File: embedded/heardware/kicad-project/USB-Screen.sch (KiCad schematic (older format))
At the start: 19 parts, among them J1 USB_B_Micro, J2 Conn_01x04, U1 ZJY154T-PG04, U2 CH551, U3 XC662

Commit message: pcb完成
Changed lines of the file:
@@
 NoConn ~ 6700 3400
 NoConn ~ 6700 3600
+Text Label 3300 1500 2    50   ~ 0
+USB_D+
 Text Label 3300 1600 2    50   ~ 0
-USB_D+
-Text Label 3300 1500 2    50   ~ 0
 USB_D-
 $Comp
 L power:GND #PWR0106
 U 1 1 5F618012
-P 3300 1700
-F 0 "#PWR0106" H 3300 1450 50  0001 C CNN
-F 1 "GND" H 3305 1527 50  0000 C CNN
-F 2 "" H 3300 1700 50  0001 C CNN
-F 3 "" H 3300 1700 50  0001 C CNN
-	1    3300 1700
-	1    0    0    -1
-$EndComp
-$Comp
-L power:+5V #PWR0105
-U 1 1 5F617214
 P 3300 1400
-F 0 "#PWR0105" H 3300 1250 50  0001 C CNN
-F 1 "+5V" V 3315 1528 50  0000 L CNN
+F 0 "#PWR0106" H 3300 1150 50  0001 C CNN
+F 1 "GND" H 3305 1227 50  0000 C CNN
 F 2 "" H 3300 1400 50  0001 C CNN
 F 3 "" H 3300 1400 50  0001 C CNN
 	1    3300 1400
-	0    1    1    0
+	0    -1   -1   0
 $EndComp
 Wire Wire Line
-	3000 1700 3300 1700
+	3300 1400 3000 1400
 Wire Wire Line
-	3000 1600 3300 1600
+	3300 1500 3000 1500
 Wire Wire Line
-	3000 1500 3300 1500
-Wire Wire Line
-	3000 1400 3300 1400
+	3300 1600 3000 1600
 Text Label 2350 1600 2    50   ~ 0
 USB_D-
@@
 	-1   0    0    1
 $EndComp
+Wire Wire Line
+	3300 1700 3000 1700
+$Comp
+L power:+5V #PWR0105
+U 1 1 5F617214
+P 3300 1700
+F 0 "#PWR0105" H 3300 1550 50  0001 C CNN
+F 1 "+5V" V 3315 1828 50  0000 L CNN
+F 2 "" H 3300 1700 50  0001 C CNN
+F 3 "" H 3300 1700 50  0001 C CNN
+	1    3300 1700
+	0    1    1    0
+$EndComp
 $EndSCHEMATC

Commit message: 微调，打样
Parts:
- U3: value XC662 -> SC662; symbol USB_Screen_Library:XC662 -> USB_Screen_Library:SC662
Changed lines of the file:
@@
 $EndComp
 $Comp
-L USB_Screen_Library:XC662 U3
+L USB_Screen_Library:SC662 U3
 U 1 1 5F61E515
 P 2000 5200
 F 0 "U3" H 2000 5400 50  0000 C CNN
-F 1 "XC662" H 2150 5000 50  0000 C CNN
+F 1 "SC662" H 2150 5000 50  0000 C CNN
 F 2 "Package_TO_SOT_SMD:SOT-23" H 2000 5350 50  0001 C CNN
 F 3 "" H 2000 5350 50  0001 C CNN

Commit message: 更正背光电路
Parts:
- added Q1: NPN, Package_TO_SOT_SMD:SOT-23, symbol Transistor_BJT:2SC4213
- added R6: 33R, Resistor_SMD:R_0402_1005Metric, symbol Device:R
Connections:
- wire segments 66 -> 71
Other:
- moved on the sheet: R2
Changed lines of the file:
@@
 L Device:R R2
 U 1 1 5F66A17C
-P 4500 3900
-F 0 "R2" V 4400 3900 50  0000 C CNN
-F 1 "33R" V 4500 3900 50  0000 C CNN
-F 2 "Resistor_SMD:R_0402_1005Metric" V 4430 3900 50  0001 C CNN
-F 3 "~" H 4500 3900 50  0001 C CNN
-	1    4500 3900
+P 4450 3900
+F 0 "R2" V 4350 3900 50  0000 C CNN
+F 1 "33R" V 4450 3900 50  0000 C CNN
+F 2 "Resistor_SMD:R_0402_1005Metric" V 4380 3900 50  0001 C CNN
+F 3 "~" H 4450 3900 50  0001 C CNN
+	1    4450 3900
 	0    -1   -1   0
 $EndComp
@@
 	1850 3950 1600 3950
 Wire Wire Line
-	4850 3900 4650 3900
-Wire Wire Line
-	4350 3900 4100 3900
-Text Label 4850 3900 2    50   ~ 0
-PWM
-Text Label 4100 3900 0    50   ~ 0
+	4300 3900 4050 3900
+Text Label 4050 3900 0    50   ~ 0
 KEDA
 Wire Wire Line
@@
 	0    1    1    0
 $EndComp
+$Comp
+L power:+5V #PWR0113
+U 1 1 5F724019
+P 4800 3900
+F 0 "#PWR0113" H 4800 3750 50  0001 C CNN
+F 1 "+5V" V 4815 4028 50  0000 L CNN
+F 2 "" H 4800 3900 50  0001 C CNN
+F 3 "" H 4800 3900 50  0001 C CNN
+	1    4800 3900
+	0    1    1    0
+$EndComp
+$Comp
+L Transistor_BJT:2SC4213 Q1
+U 1 1 5F727A10
+P 4500 4600
+F 0 "Q1" H 4691 4554 50  0000 L CNN
+F 1 "NPN" H 4691 4645 50  0000 L CNN
+F 2 "Package_TO_SOT_SMD:SOT-23" H 4700 4525 50  0001 L CIN
+F 3 "https://toshiba.semicon-storage.com/info/docget.jsp?did=19305&prodName=2SC4213" H 4500 4600 50  0001 L CNN
+	1    4500 4600
+	-1   0    0    1
+$EndComp
+$Comp
+L power:+5V #PWR0114
+U 1 1 5F730CBA
+P 4400 5000
+F 0 "#PWR0114" H 4400 4850 50  0001 C CNN
+F 1 "+5V" H 4415 5173 50  0000 C CNN
+F 2 "" H 4400 5000 50  0001 C CNN
+F 3 "" H 4400 5000 50  0001 C CNN
+	1    4400 5000
+	-1   0    0    1
+$EndComp
+Wire Wire Line
+	4400 5000 4400 4800
+Wire Wire Line
+	4800 3900 4600 3900
+Wire Wire Line
+	4400 4250 4400 4400
+Wire Wire Line
+	4700 4600 5000 4600
+Text Label 5000 4600 2    50   ~ 0
+PWM
+Text Label 3450 4250 0    50   ~ 0
+KEDA
+$Comp
+L Device:R R6
+U 1 1 5F74A98E
+P 4000 4250
+F 0 "R6" V 3900 4250 50  0000 C CNN
+F 1 "33R" V 4000 4250 50  0000 C CNN
+F 2 "Resistor_SMD:R_0402_1005Metric" V 3930 4250 50  0001 C CNN
+F 3 "~" H 4000 4250 50  0001 C CNN
+	1    4000 4250
+	0    -1   -1   0
+$EndComp
+Wire Wire Line
+	3450 4250 3850 4250
+Wire Wire Line
+	4150 4250 4400 4250
 $EndSCHEMATC

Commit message: sda、clk加上拉电阻，去掉下载电路焊盘
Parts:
- removed JP1: P3.6 download, Jumper:SolderJumper-2_P1.3mm_Open_Pad1.0x1.5mm, symbol Device:Jumper_NO_Small
- added R7: 10K, Resistor_SMD:R_0402_1005Metric, symbol Device:R
- Q1: symbol Transistor_BJT:2SC4213 -> USB-Screen-rescue:2SC4213-Transistor_BJT
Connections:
- wire segments 71 -> 70
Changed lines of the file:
@@
 EESchema Schematic File Version 4
+LIBS:USB-Screen-cache
 EELAYER 30 0
 EELAYER END
@@
 PWM
 $Comp
-L Device:Jumper_NO_Small JP1
-U 1 1 5F656264
-P 6850 2000
-F 0 "JP1" H 6850 2100 50  0000 C CNN
-F 1 "P3.6 download" H 6800 1950 50  0000 C CNN
-F 2 "Jumper:SolderJumper-2_P1.3mm_Open_Pad1.0x1.5mm" H 6850 2000 50  0001 C CNN
-F 3 "~" H 6850 2000 50  0001 C CNN
-	1    6850 2000
-	1    0    0    -1
-$EndComp
-Wire Wire Line
-	6500 2000 6750 2000
-Wire Wire Line
-	6950 2000 7100 2000
-Text Label 6500 2000 0    50   ~ 0
-USB_D+
-$Comp
-L Device:R R1
-U 1 1 5F662FAB
-P 7250 2000
-F 0 "R1" V 7350 2000 50  0000 C CNN
-F 1 "10K" V 7250 2000 50  0000 C CNN
-F 2 "Resistor_SMD:R_0402_1005Metric" V 7180 2000 50  0001 C CNN
-F 3 "~" H 7250 2000 50  0001 C CNN
-	1    7250 2000
-	0    -1   -1   0
-$EndComp
-$Comp
-L power:+5V #PWR08
-U 1 1 5F663B6A
-P 7600 2000
-F 0 "#PWR08" H 7600 1850 50  0001 C CNN
-F 1 "+5V" V 7615 2128 50  0000 L CNN
-F 2 "" H 7600 2000 50  0001 C CNN
-F 3 "" H 7600 2000 50  0001 C CNN
-	1    7600 2000
-	0    1    1    0
-$EndComp
-Wire Wire Line
-	7400 2000 7600 2000
-$Comp
 L Device:R R2
 U 1 1 5F66A17C
@@
 $EndComp
 $Comp
-L Transistor_BJT:2SC4213 Q1
+L USB-Screen-rescue:2SC4213-Transistor_BJT Q1
 U 1 1 5F727A10
 P 4500 4600
@@
 Wire Wire Line
 	4150 4250 4400 4250
+$Comp
+L Device:R R1
+U 1 1 5F81BAD2
+P 2750 3100
+F 0 "R1" H 2680 3054 50  0000 R CNN
+F 1 "10K" H 2680 3145 50  0000 R CNN
+F 2 "Resistor_SMD:R_0402_1005Metric" V 2680 3100 50  0001 C CNN
+F 3 "~" H 2750 3100 50  0001 C CNN
+	1    2750 3100
+	-1   0    0    1
+$EndComp
+$Comp
+L Device:R R7
+U 1 1 5F81D793
+P 3000 3100
+F 0 "R7" H 3070 3146 50  0000 L CNN
+F 1 "10K" H 3070 3055 50  0000 L CNN
+F 2 "Resistor_SMD:R_0402_1005Metric" V 2930 3100 50  0001 C CNN
+F 3 "~" H 3000 3100 50  0001 C CNN
+	1    3000 3100
+	1    0    0    -1
+$EndComp
+$Comp
+L power:+3.3V #PWR0115
+U 1 1 5F8207AA
+P 2750 2950
+F 0 "#PWR0115" H 2750 2800 50  0001 C CNN
+F 1 "+3.3V" H 2765 3123 50  0000 C CNN
+F 2 "" H 2750 2950 50  0001 C CNN
+F 3 "" H 2750 2950 50  0001 C CNN
+	1    2750 2950
+	1    0    0    -1
+$EndComp
+$Comp
+L power:+3.3V #PWR0116
+U 1 1 5F820FDB
+P 3000 2950
+F 0 "#PWR0116" H 3000 2800 50  0001 C CNN
+F 1 "+3.3V" H 3015 3123 50  0000 C CNN
+F 2 "" H 3000 2950 50  0001 C CNN
+F 3 "" H 3000 2950 50  0001 C CNN
+	1    3000 2950
+	1    0    0    -1
+$EndComp
+Wire Wire Line
+	2750 3250 2750 3500
+Wire Wire Line
+	3000 3250 3000 3500
+Text Label 2750 3500 1    50   ~ 0
+SCL
+Text Label 3000 3500 1    50   ~ 0
+SDA
 $EndSCHEMATC

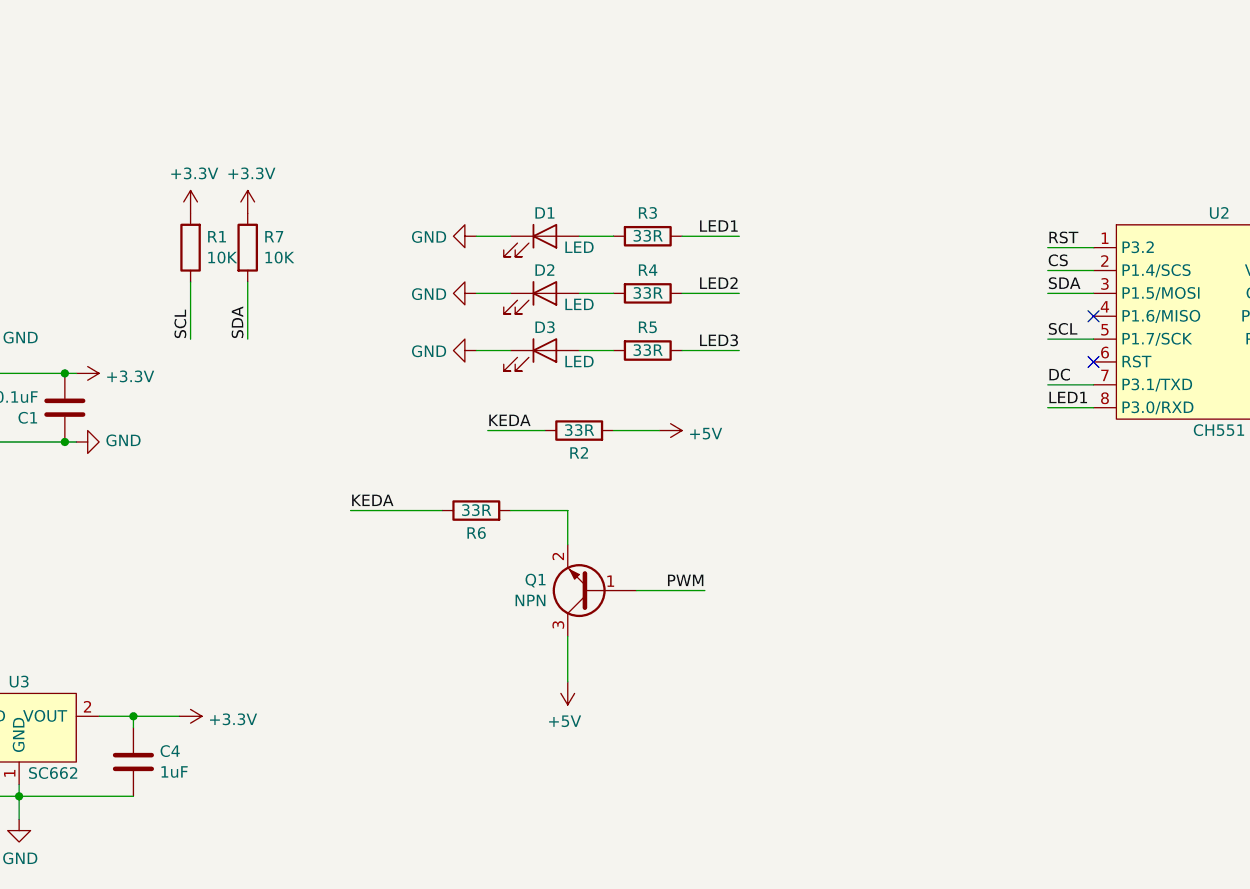
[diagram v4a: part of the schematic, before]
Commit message: 修改SPI总线分压电路
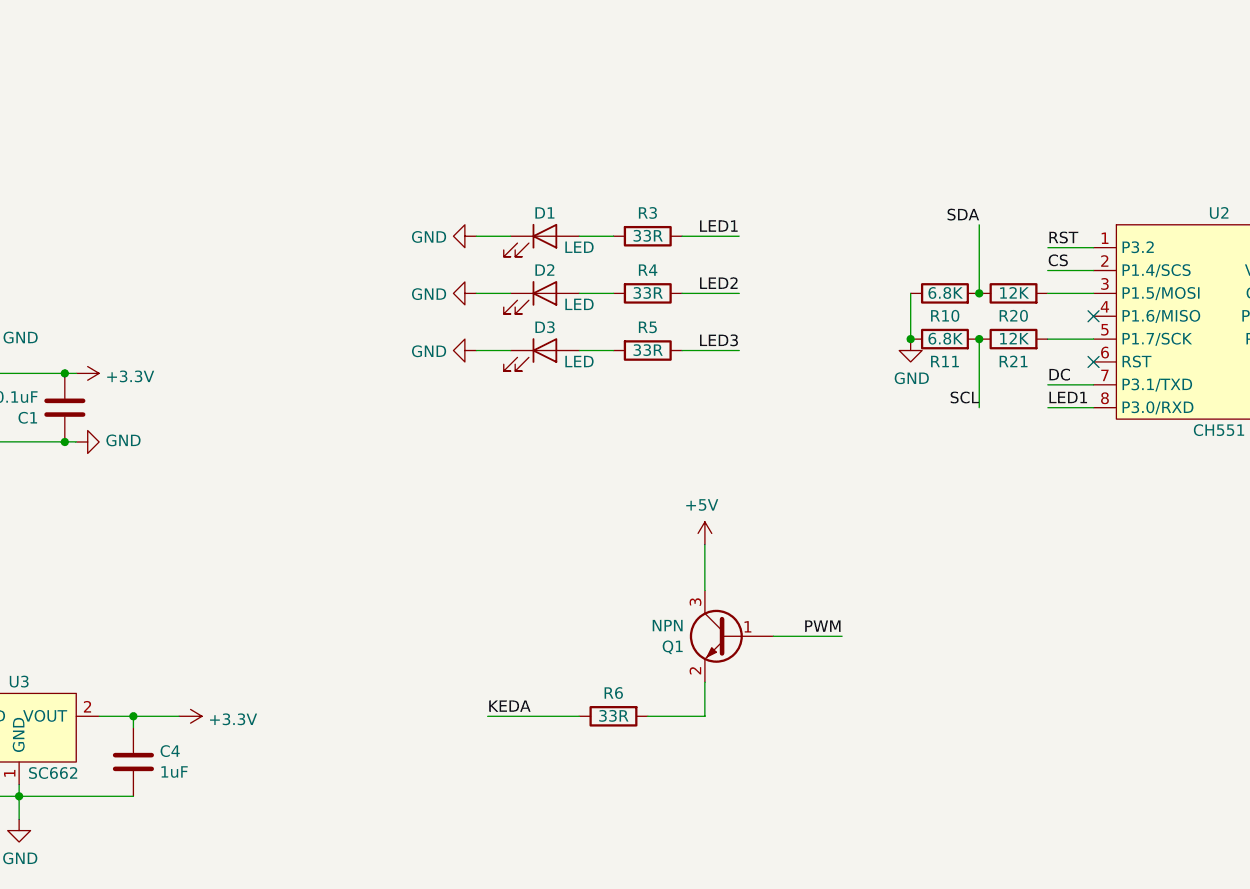
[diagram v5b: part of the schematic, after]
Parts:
- removed R1, R7: 10K, Resistor_SMD:R_0402_1005Metric, symbol Device:R
- removed R2: 33R, Resistor_SMD:R_0402_1005Metric, symbol Device:R
- added R10, R11: 6.8K, Resistor_SMD:R_0402_1005Metric, symbol Device:R
- added R20, R21: 12K, Resistor_SMD:R_0402_1005Metric, symbol Device:R
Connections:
- net GND: now also R10.1, R11.1
- net SCL: now also R11.2, R21.1; no longer U2.5 (P1.7/SCK)
- net SDA: now also R10.2, R20.1; no longer U2.3 (P1.5/MOSI)
- new net: R20.2, U2.3 (P1.5/MOSI)
- new net: R21.2, U2.5 (P1.7/SCK)
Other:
- moved on the sheet: Q1, R6
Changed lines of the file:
@@
 EESchema Schematic File Version 4
-LIBS:USB-Screen-cache
 EELAYER 30 0
 EELAYER END
@@
 Text Label 6500 3200 0    50   ~ 0
 CS
-Text Label 6500 3300 0    50   ~ 0
-SDA
-Text Label 6500 3500 0    50   ~ 0
-SCL
 Wire Wire Line
 	8200 3600 7800 3600
@@
 Text Label 8200 3600 2    50   ~ 0
 PWM
-$Comp
-L Device:R R2
-U 1 1 5F66A17C
-P 4450 3900
-F 0 "R2" V 4350 3900 50  0000 C CNN
-F 1 "33R" V 4450 3900 50  0000 C CNN
-F 2 "Resistor_SMD:R_0402_1005Metric" V 4380 3900 50  0001 C CNN
-F 3 "~" H 4450 3900 50  0001 C CNN
-	1    4450 3900
-	0    -1   -1   0
-$EndComp
 Wire Wire Line
 	1850 3850 1850 3950
@@
 Wire Wire Line
 	1850 3950 1600 3950
-Wire Wire Line
-	4300 3900 4050 3900
-Text Label 4050 3900 0    50   ~ 0
-KEDA
 Wire Wire Line
 	6500 3100 6700 3100
@@
 $EndComp
 $Comp
-L power:+5V #PWR0113
-U 1 1 5F724019
-P 4800 3900
-F 0 "#PWR0113" H 4800 3750 50  0001 C CNN
-F 1 "+5V" V 4815 4028 50  0000 L CNN
-F 2 "" H 4800 3900 50  0001 C CNN
-F 3 "" H 4800 3900 50  0001 C CNN
-	1    4800 3900
-	0    1    1    0
-$EndComp
-$Comp
 L USB-Screen-rescue:2SC4213-Transistor_BJT Q1
 U 1 1 5F727A10
-P 4500 4600
-F 0 "Q1" H 4691 4554 50  0000 L CNN
-F 1 "NPN" H 4691 4645 50  0000 L CNN
-F 2 "Package_TO_SOT_SMD:SOT-23" H 4700 4525 50  0001 L CIN
-F 3 "https://toshiba.semicon-storage.com/info/docget.jsp?did=19305&prodName=2SC4213" H 4500 4600 50  0001 L CNN
-	1    4500 4600
-	-1   0    0    1
+P 5100 4800
+F 0 "Q1" H 5291 4754 50  0000 L CNN
+F 1 "NPN" H 5291 4845 50  0000 L CNN
+F 2 "Package_TO_SOT_SMD:SOT-23" H 5300 4725 50  0001 L CIN
+F 3 "https://toshiba.semicon-storage.com/info/docget.jsp?did=19305&prodName=2SC4213" H 5100 4800 50  0001 L CNN
+	1    5100 4800
+	-1   0    0    -1
 $EndComp
 $Comp
 L power:+5V #PWR0114
 U 1 1 5F730CBA
-P 4400 5000
-F 0 "#PWR0114" H 4400 4850 50  0001 C CNN
-F 1 "+5V" H 4415 5173 50  0000 C CNN
-F 2 "" H 4400 5000 50  0001 C CNN
-F 3 "" H 4400 5000 50  0001 C CNN
-	1    4400 5000
-	-1   0    0    1
-$EndComp
-Wire Wire Line
-	4400 5000 4400 4800
-Wire Wire Line
-	4800 3900 4600 3900
-Wire Wire Line
-	4400 4250 4400 4400
-Wire Wire Line
-	4700 4600 5000 4600
-Text Label 5000 4600 2    50   ~ 0
+P 5000 4400
+F 0 "#PWR0114" H 5000 4250 50  0001 C CNN
+F 1 "+5V" H 5015 4573 50  0000 C CNN
+F 2 "" H 5000 4400 50  0001 C CNN
+F 3 "" H 5000 4400 50  0001 C CNN
+	1    5000 4400
+	-1   0    0    -1
+$EndComp
+Wire Wire Line
+	5000 4400 5000 4600
+Wire Wire Line
+	5000 5150 5000 5000
+Wire Wire Line
+	5300 4800 5600 4800
+Text Label 5600 4800 2    50   ~ 0
 PWM
-Text Label 3450 4250 0    50   ~ 0
+Text Label 4050 5150 0    50   ~ 0
 KEDA
 $Comp
 L Device:R R6
 U 1 1 5F74A98E
-P 4000 4250
-F 0 "R6" V 3900 4250 50  0000 C CNN
-F 1 "33R" V 4000 4250 50  0000 C CNN
-F 2 "Resistor_SMD:R_0402_1005Metric" V 3930 4250 50  0001 C CNN
-F 3 "~" H 4000 4250 50  0001 C CNN
-	1    4000 4250
-	0    -1   -1   0
-$EndComp
-Wire Wire Line
-	3450 4250 3850 4250
-Wire Wire Line
-	4150 4250 4400 4250
-$Comp
-L Device:R R1
-U 1 1 5F81BAD2
-P 2750 3100
-F 0 "R1" H 2680 3054 50  0000 R CNN
-F 1 "10K" H 2680 3145 50  0000 R CNN
-F 2 "Resistor_SMD:R_0402_1005Metric" V 2680 3100 50  0001 C CNN
-F 3 "~" H 2750 3100 50  0001 C CNN
-	1    2750 3100
-	-1   0    0    1
-$EndComp
-$Comp
-L Device:R R7
-U 1 1 5F81D793
-P 3000 3100
-F 0 "R7" H 3070 3146 50  0000 L CNN
-F 1 "10K" H 3070 3055 50  0000 L CNN
-F 2 "Resistor_SMD:R_0402_1005Metric" V 2930 3100 50  0001 C CNN
-F 3 "~" H 3000 3100 50  0001 C CNN
-	1    3000 3100
-	1    0    0    -1
-$EndComp
-$Comp
-L power:+3.3V #PWR0115
-U 1 1 5F8207AA
-P 2750 2950
-F 0 "#PWR0115" H 2750 2800 50  0001 C CNN
-F 1 "+3.3V" H 2765 3123 50  0000 C CNN
-F 2 "" H 2750 2950 50  0001 C CNN
-F 3 "" H 2750 2950 50  0001 C CNN
-	1    2750 2950
-	1    0    0    -1
-$EndComp
-$Comp
-L power:+3.3V #PWR0116
-U 1 1 5F820FDB
-P 3000 2950
-F 0 "#PWR0116" H 3000 2800 50  0001 C CNN
-F 1 "+3.3V" H 3015 3123 50  0000 C CNN
-F 2 "" H 3000 2950 50  0001 C CNN
-F 3 "" H 3000 2950 50  0001 C CNN
-	1    3000 2950
-	1    0    0    -1
-$EndComp
-Wire Wire Line
-	2750 3250 2750 3500
-Wire Wire Line
-	3000 3250 3000 3500
-Text Label 2750 3500 1    50   ~ 0
+P 4600 5150
+F 0 "R6" V 4500 5150 50  0000 C CNN
+F 1 "33R" V 4600 5150 50  0000 C CNN
+F 2 "Resistor_SMD:R_0402_1005Metric" V 4530 5150 50  0001 C CNN
+F 3 "~" H 4600 5150 50  0001 C CNN
+	1    4600 5150
+	0    -1   1    0
+$EndComp
+Wire Wire Line
+	4050 5150 4450 5150
+Wire Wire Line
+	4750 5150 5000 5150
+$Comp
+L Device:R R20
+U 1 1 5F8499B6
+P 6350 3300
+F 0 "R20" V 6250 3300 50  0000 C CNN
+F 1 "12K" V 6350 3300 50  0000 C CNN
+F 2 "Resistor_SMD:R_0402_1005Metric" V 6280 3300 50  0001 C CNN
+F 3 "~" H 6350 3300 50  0001 C CNN
+	1    6350 3300
+	0    -1   -1   0
+$EndComp
+$Comp
+L Device:R R10
+U 1 1 5F84B636
+P 6050 3300
+F 0 "R10" V 5950 3300 50  0000 C CNN
+F 1 "6.8K" V 6050 3300 50  0000 C CNN
+F 2 "Resistor_SMD:R_0402_1005Metric" V 5980 3300 50  0001 C CNN
+F 3 "~" H 6050 3300 50  0001 C CNN
+	1    6050 3300
+	0    -1   -1   0
+$EndComp
+Text Label 6200 3000 2    50   ~ 0
+SDA
+$Comp
+L Device:R R21
+U 1 1 5F852FA8
+P 6350 3500
+F 0 "R21" V 6250 3500 50  0000 C CNN
+F 1 "12K" V 6350 3500 50  0000 C CNN
+F 2 "Resistor_SMD:R_0402_1005Metric" V 6280 3500 50  0001 C CNN
+F 3 "~" H 6350 3500 50  0001 C CNN
+	1    6350 3500
+	0    -1   -1   0
+$EndComp
+$Comp
+L Device:R R11
+U 1 1 5F852FB2
+P 6050 3500
+F 0 "R11" V 5950 3500 50  0000 C CNN
+F 1 "6.8K" V 6050 3500 50  0000 C CNN
+F 2 "Resistor_SMD:R_0402_1005Metric" V 5980 3500 50  0001 C CNN
+F 3 "~" H 6050 3500 50  0001 C CNN
+	1    6050 3500
+	0    -1   -1   0
+$EndComp
+$Comp
+L power:GND #PWR?
+U 1 1 5F852FBC
+P 5900 3500
+F 0 "#PWR?" H 5900 3250 50  0001 C CNN
+F 1 "GND" H 5905 3327 50  0000 C CNN
+F 2 "" H 5900 3500 50  0001 C CNN
+F 3 "" H 5900 3500 50  0001 C CNN
+	1    5900 3500
+	1    0    0    -1
+$EndComp
+Wire Wire Line
+	6200 3000 6200 3300
+Connection ~ 6200 3300
+Connection ~ 6200 3500
+Text Label 6200 3800 2    50   ~ 0
 SCL
-Text Label 3000 3500 1    50   ~ 0
-SDA
+Wire Wire Line
+	6200 3500 6200 3800
+Wire Wire Line
+	5900 3300 5900 3500
+Connection ~ 5900 3500
 $EndSCHEMATC
